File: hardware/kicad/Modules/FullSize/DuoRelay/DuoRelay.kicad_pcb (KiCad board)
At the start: 2 copper layers, 38 x 64 mm, 15 parts, among them J1 Conn_02x07_Odd_Even, K1 FINDER-34.51.7.005.0010, K2 FINDER-34.51.7.005.0010, Q1 BC817, Q2 BC817

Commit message: Reorganize module projects and add identification EEPROMs
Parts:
- added C1: 100nF, Capacitor_SMD:C_1206_3216Metric_Pad1.33x1.80mm_HandSolder, B.Cu at (151.0, 36.8)
- added U1: 24AA025E-OT, Package_TO_SOT_SMD:SOT-23-6, B.Cu at (151.0, 39.8)
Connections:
- net /GND renamed GND
- J1 pad 2: /+3V3_SYS -> +3V3_SYS
- J1 pad 5: /I2C0_SDA -> I2C0_SDA
- J1 pad 6: /I2C0_SCL -> I2C0_SCL
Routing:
- net +3V3_SYS: track 0.00 -> 32.1 mm
- net /EEPROM_A0: track 0.00 -> 22.9 mm
- net I2C0_SDA: track 0.00 -> 16.2 mm
- net I2C0_SCL: track 0.00 -> 16.2 mm
- net /AUX_GPIO1: track 10.7 -> 13.2 mm
- net GND: vias 0 -> 1

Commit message: Add relay status LEDs to DuoRelay
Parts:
- added D3: LED, LED_SMD:LED_1206_3216Metric_Pad1.42x1.75mm_HandSolder, F.Cu at (121.8, 45.6)
- added D4: LED, LED_SMD:LED_1206_3216Metric_Pad1.42x1.75mm_HandSolder, F.Cu at (151.6, 45.6)
- added R5: 1,5kO, LED_SMD:LED_1206_3216Metric_Pad1.42x1.75mm_HandSolder, F.Cu at (121.8, 49.9)
- added R6: 1,5kO, Resistor_SMD:R_1206_3216Metric_Pad1.30x1.75mm_HandSolder, F.Cu at (151.6, 49.9)
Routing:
- net /+5V: track 49.5 -> 78.5 mm
- net Net-(D4-K): track 0.00 -> 4.33 mm
- net Net-(D3-K): track 0.00 -> 4.31 mm
- net Net-(D1-A): track 8.79 -> 13.0 mm
- net Net-(D2-A): track 11.5 -> 15.1 mm
- net GND: vias 1 -> 2

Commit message: Fix EEPROM values and DuoRelay R5 footprint
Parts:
- R5: footprint LED_SMD:LED_1206_3216Metric_Pad1.42x1.75mm_HandSolder -> Resistor_SMD:R_1206_3216Metric_Pad1.30x1.75mm_HandSolder
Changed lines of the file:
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@@
 		)
 	)
-	(footprint "LED_SMD:LED_1206_3216Metric_Pad1.42x1.75mm_HandSolder"
+	(footprint "Resistor_SMD:R_1206_3216Metric_Pad1.30x1.75mm_HandSolder"
 		(layer "F.Cu")
 		(at 121.805 49.86 180)
-		(descr "LED SMD 1206 (3216 Metric), square (rectangular) end terminal, IPC-7351 nominal, (Body size source: http://www.tortai-tech.com/upload/download/2011102023233369053.pdf)")
-		(tags "LED handsolder")
+		(descr "Resistor SMD 1206 (3216 Metric), square (rectangular) end terminal, IPC-7351 nominal with elongated pad for handsoldering. (Body size source: IPC-SM-782 page 72, https://www.pcb-3d.com/wordpress/wp-content/uploads/ipc-sm-782a_amendment_1_and_2.pdf)")
+		(tags "resistor handsolder")
 		(property "Reference" "R5"
-			(at 0 1.82 0)
+			(at 0 -1.83 180)
 			(layer "F.SilkS")
 			(effects
@@
 		)
 		(property "Value" "1,5kO"
-			(at 0 1.83 0)
+			(at 0 1.83 180)
 			(layer "F.Fab")
 			(effects
@@
 		)
 		(property "Datasheet" ""
-			(at 0 0 0)
+			(at 0 0 180)
 			(layer "F.Fab")
 			(hide yes)
@@
 		)
 		(property "Description" "Resistor"
-			(at 0 0 0)
+			(at 0 0 180)
 			(layer "F.Fab")
 			(hide yes)
@@
 		)
 		(property "KiLib_Generator" "SMD_2terminal_chip_molded"
-			(at 0 0 0)
+			(at 0 0 180)
 			(layer "F.SilkS")
 			(hide yes)
@@
 		(duplicate_pad_numbers_are_jumpers no)
 		(fp_line
-			(start 1.6 -1.135)
-			(end -2.46 -1.135)
-			(stroke
-				(width 0.12)
-				(type solid)
-			)
-			(layer "F.SilkS")
-		)
-		(fp_line
-			(start -2.46 1.135)
-			(end 1.6 1.135)
+			(start -0.727064 0.91)
+			(end 0.727064 0.91)
 			(stroke
 				(width 0.12)
@@
 		)
 		(fp_line
-			(start -2.46 -1.135)
-			(end -2.46 1.135)
+			(start -0.727064 -0.91)
+			(end 0.727064 -0.91)
 			(stroke
 				(width 0.12)
@@
 			(layer "F.CrtYd")
 		)
-		(fp_line
-			(start 1.6 0.8)
-			(end 1.6 -0.8)
-			(stroke
-				(width 0.1)
-				(type solid)
-			)
-			(layer "F.Fab")
-		)
-		(fp_line
-			(start 1.6 -0.8)
-			(end -1.2 -0.8)
-			(stroke
-				(width 0.1)
-				(type solid)
-			)
-			(layer "F.Fab")
-		)
-		(fp_line
-			(start -1.2 -0.8)
-			(end -1.6 -0.4)
-			(stroke
-				(width 0.1)
-				(type solid)
-			)
-			(layer "F.Fab")
-		)
-		(fp_line
-			(start -1.6 0.8)
+		(fp_rect
+			(start -1.6 -0.8)
 			(end 1.6 0.8)
 			(stroke
@@
 				(type solid)
 			)
-			(layer "F.Fab")
-		)
-		(fp_line
-			(start -1.6 -0.4)
-			(end -1.6 0.8)
-			(stroke
-				(width 0.1)
-				(type solid)
-			)
+			(fill no)
 			(layer "F.Fab")
 		)
 		(fp_text user "${REFERENCE}"
-			(at 0 0 0)
+			(at 0 0 180)
 			(layer "F.Fab")
 			(effects
@@
 		)
 		(pad "1" smd roundrect
-			(at -1.4875 0 180)
-			(size 1.425 1.75)
+			(at -1.55 0 180)
+			(size 1.3 1.75)
 			(layers "F.Cu" "F.Mask" "F.Paste")
-			(roundrect_rratio 0.175439)
+			(roundrect_rratio 0.192308)
 			(net "Net-(D1-A)")
 			(pintype "passive")
 		)
 		(pad "2" smd roundrect
-			(at 1.4875 0 180)
-			(size 1.425 1.75)
+			(at 1.55 0 180)
+			(size 1.3 1.75)
 			(layers "F.Cu" "F.Mask" "F.Paste")
-			(roundrect_rratio 0.175439)
+			(roundrect_rratio 0.192308)
 			(net "Net-(D3-K)")
 			(pintype "passive")
 		)
 		(embedded_fonts no)
-		(model "${KICAD10_3DMODEL_DIR}/LED_SMD.3dshapes/LED_1206_3216Metric.step"
+		(model "${KICAD10_3DMODEL_DIR}/Resistor_SMD.3dshapes/R_1206_3216Metric.step"
 			(offset
 				(xyz 0 0 0)
@@
 	)
 	(segment
+		(start 120.3175 45.615)
+		(end 120.3625 45.57)
+		(width 0.2)
+		(layer "F.Cu")
+		(net "Net-(D3-K)")
+	)
+	(segment
+		(start 120.3175 49.86)
+		(end 120.3175 45.615)
+		(width 0.2)
+		(layer "F.Cu")
+		(net "Net-(D3-K)")
+	)
+	(segment
 		(start 140.07 40.633)
 		(end 139.319 39.882)
@@
 	)
 	(segment
+		(start 153.1575 49.86)
+		(end 153.1575 45.655)
+		(width 0.2)
+		(layer "F.Cu")
+		(net "Net-(D4-K)")
+	)
+	(segment
+		(start 153.1575 45.655)
+		(end 153.0725 45.57)
+		(width 0.2)
+		(layer "F.Cu")
+		(net "Net-(D4-K)")
+	)
+	(segment
 		(start 152.0975 41.1325)
 		(end 152.0975 40.73)
@@
 		(net "I2C0_SCL")
 	)
-	(segment
-		(start 120.3175 45.615)
-		(end 120.3625 45.57)
-		(width 0.2)
-		(layer "F.Cu")
-		(net "Net-(D3-K)")
-	)
-	(segment
-		(start 120.3175 49.86)
-		(end 120.3175 45.615)
-		(width 0.2)
-		(layer "F.Cu")
-		(net "Net-(D3-K)")
-	)
-	(segment
-		(start 153.1575 49.86)
-		(end 153.1575 45.655)
-		(width 0.2)
-		(layer "F.Cu")
-		(net "Net-(D4-K)")
-	)
-	(segment
-		(start 153.1575 45.655)
-		(end 153.0725 45.57)
-		(width 0.2)
-		(layer "F.Cu")
-		(net "Net-(D4-K)")
-	)
 	(zone

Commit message: Finalize DuoRelay Rev 0.2 assembly package
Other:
- board text added: "NC COM NO"
- board text added: "NO COM NC"
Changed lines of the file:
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@@
 			(outputformat 1)
 			(mirror no)
-			(drillshape 1)
+			(drillshape 0)
 			(scaleselection 1)
-			(outputdirectory "")
+			(outputdirectory "Gerber")
 		)
 	)
@@
 		)
 	)
+	(gr_text "NO COM NC"
+		(at 119.112142 83.58 0)
+		(layer "F.SilkS")
+		(effects
+			(font
+				(size 1.5 1.5)
+				(thickness 0.3)
+				(bold yes)
+			)
+			(justify left bottom)
+		)
+	)
+	(gr_text "NC COM NO"
+		(at 140.567142 83.58 0)
+		(layer "F.SilkS")
+		(effects
+			(font
+				(size 1.5 1.5)
+				(thickness 0.3)
+				(bold yes)
+			)
+			(justify left bottom)
+		)
+	)

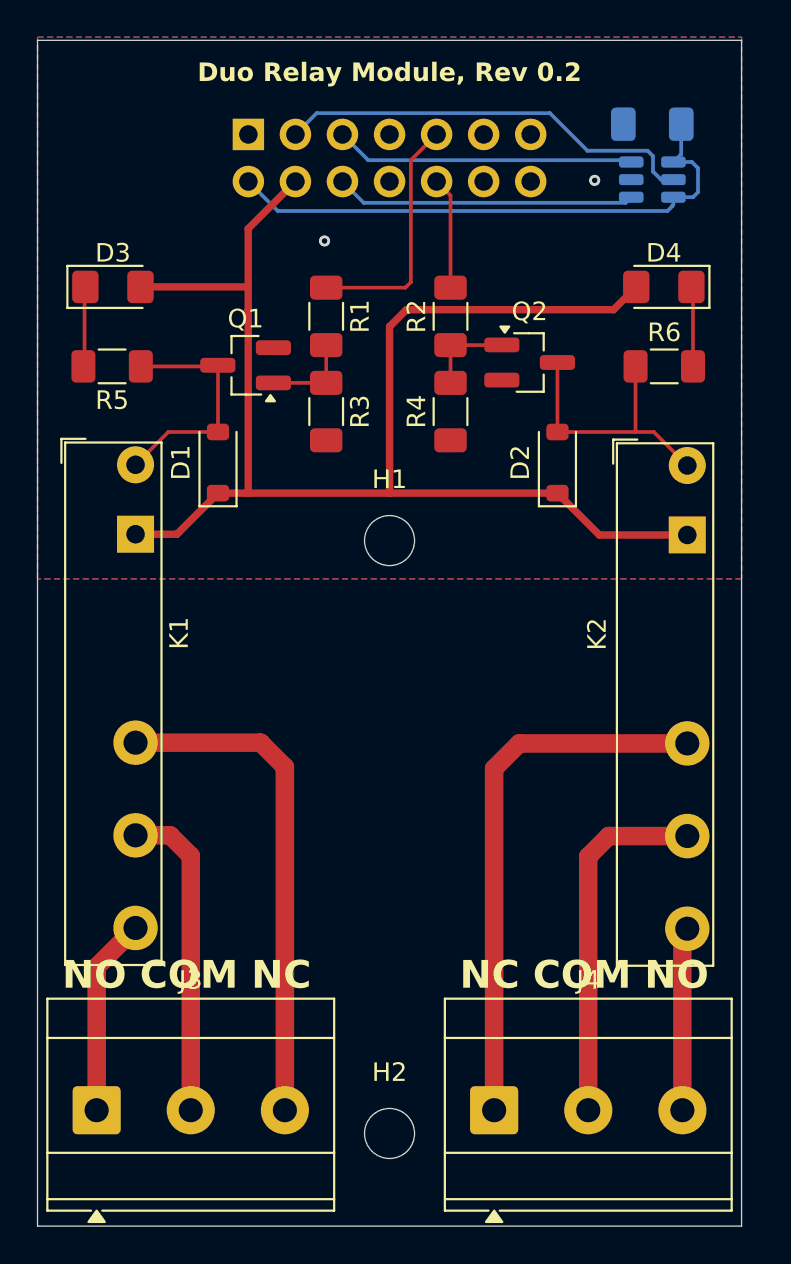
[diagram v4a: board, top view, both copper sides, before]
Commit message: Update module layouts for Rev 0.3
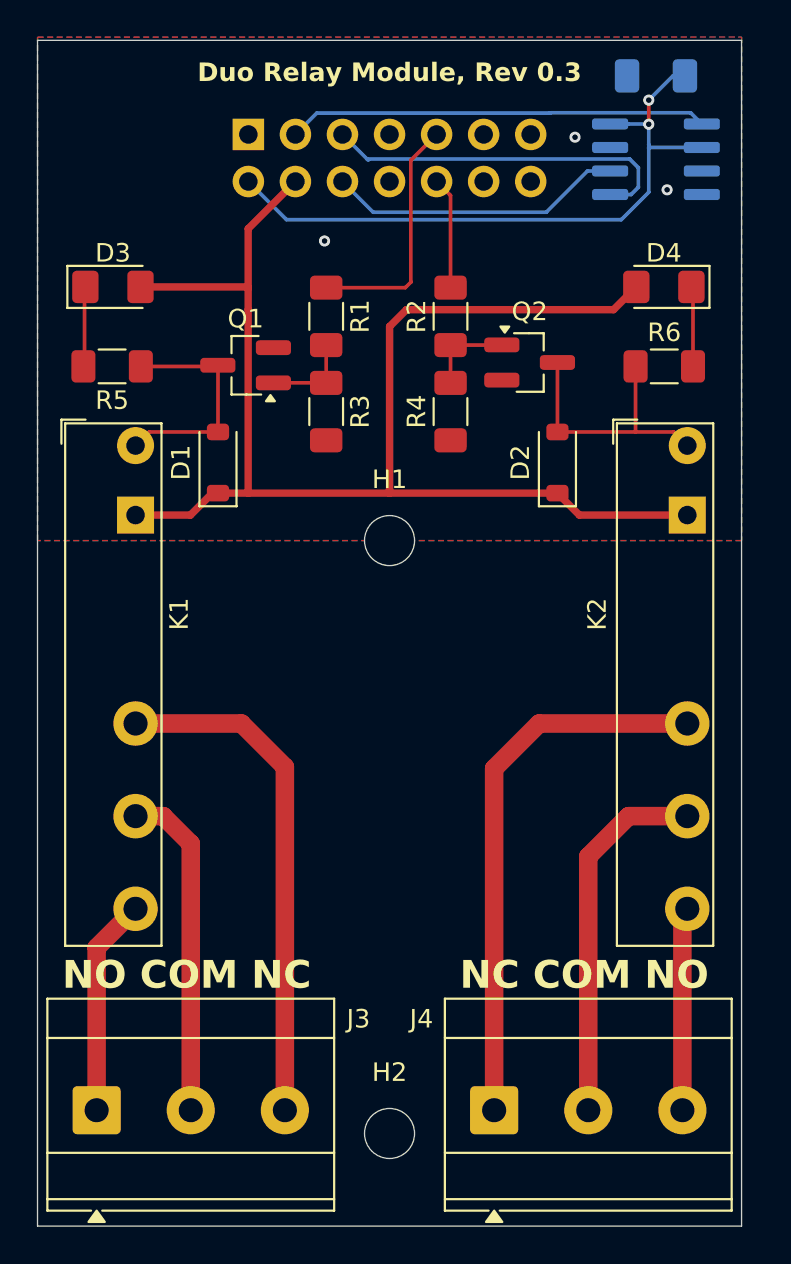
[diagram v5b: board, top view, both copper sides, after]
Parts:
- removed U1: 24AA025E-OT, Package_TO_SOT_SMD:SOT-23-6
- added U2: 24LC32, Package_SO:SOIC-8_3.9x4.9mm_P1.27mm, B.Cu at (151.2, 38.7)
- moved C1 2.62 mm to (151.2, 34.2)
- moved K2 1.08 mm to (152.8, 57.9)
- moved K1 1.04 mm to (123.1, 57.9)
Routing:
- net +3V3_SYS: track 32.1 -> 38.1 mm, vias 0 -> 2
- net I2C0_SDA: track 16.2 -> 19.5 mm
- net /NO2: track 9.91 -> 11.0 mm
- net /NO1: track 10.7 -> 11.7 mm
- net /+5V: track 78.5 -> 77.7 mm
- net /COM1: track 17.2 -> 18.0 mm
- net GND: vias 2 -> 3
